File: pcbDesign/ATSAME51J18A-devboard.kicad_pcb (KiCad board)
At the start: 2 copper layers, 82.3 x 28.4 mm, 74 parts, among them J1 Micro_SD_Card, J10 CAN, J11 Conn_01x32_Male, J2 BAT, J3 QWIIC, J7 Conn_01x32_Male, J9 USB4105_REVA, SW1 RST, U1 TCAN1051GVDRQ1, U2 ATSAME51J18A-A, U3 MIC5219-5.0YMM, U4 LM27762, U5 LM2775QDSGTQ1, U6 SC630AULTRT, U7 BQ24074RGT, U8 BQ27441DRZR-G1B, Y1 32.768

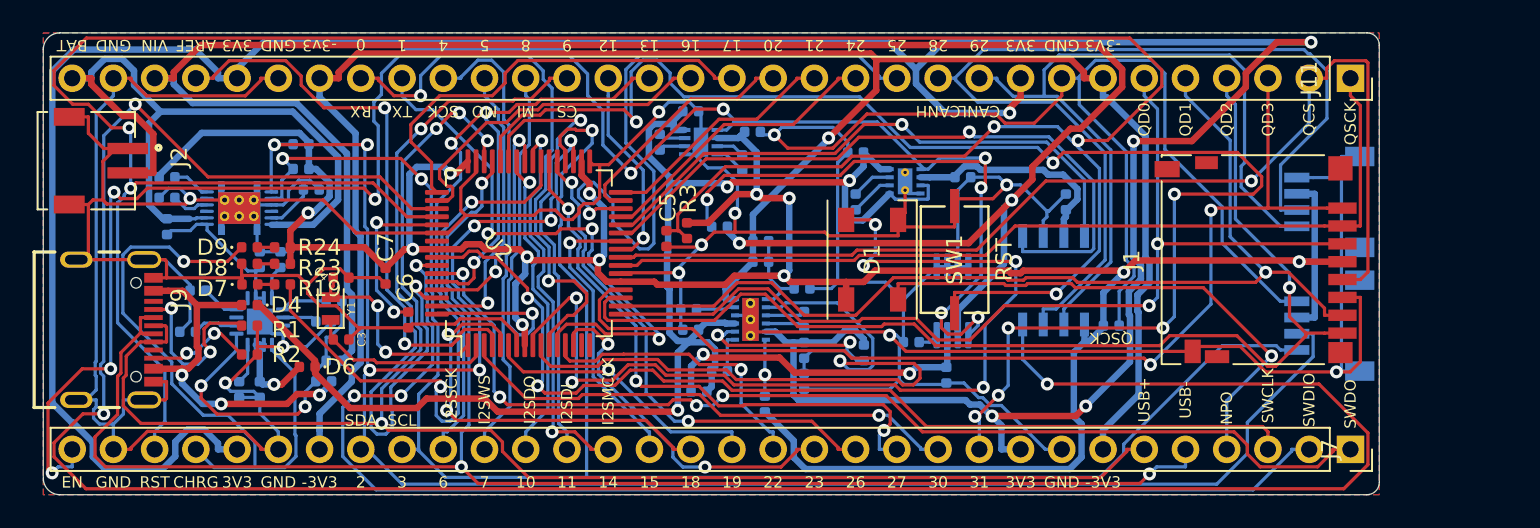
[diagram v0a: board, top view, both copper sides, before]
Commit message: Rewired SD card to SPI for ease of use
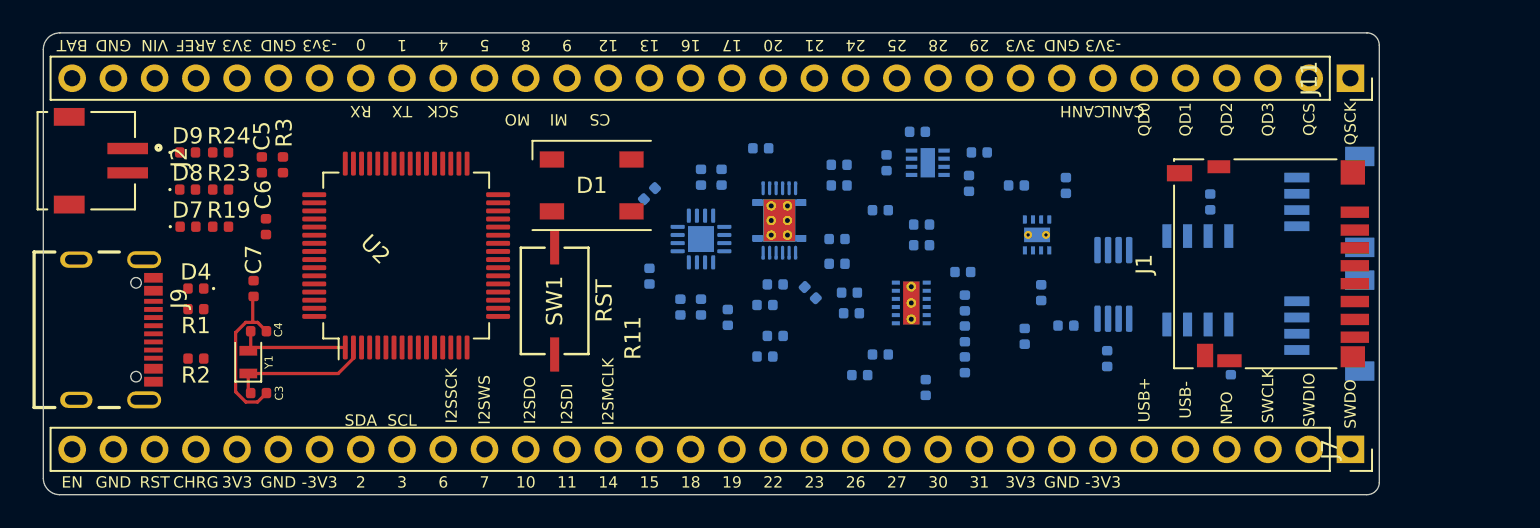
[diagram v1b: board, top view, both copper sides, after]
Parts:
- D6: moved to B.Cu
- moved R17 41.5 mm to (190.0, 119.6), turned to 0 degrees
- moved R18 41.4 mm to (190.0, 120.9), turned to 0 degrees
- moved R16 36.9 mm to (185.2, 118.6), turned to 0 degrees
- moved R14 33.5 mm to (189.9, 124.2)
- moved R15 33.5 mm to (189.9, 125.7)
- moved U8 33.3 mm to (186.3, 123.1), turned to 90 degrees
- moved C24 31.4 mm to (188.2, 127.5), turned to 315 degrees
- moved R11 28.7 mm to (178.3, 126.5), turned to 90 degrees
- moved R13 28.4 mm to (178.3, 121.4), turned to 45 degrees
- moved C22 27.6 mm to (181.5, 128.4)
- moved C23 27.6 mm to (181.5, 120.4)
- moved R22 27.6 mm to (182.8, 120.4)
- moved U7 27.6 mm to (181.5, 124.2)
- moved R12 27.6 mm to (180.2, 128.4)
- moved D2 27.2 mm to (185.4, 131.4)
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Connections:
- J1 pad 1: QDAT3 -> (no net)
- J1 pad 2: QSCK -> SDDAT3
- J1 pad 3: QDAT0 -> 5[MO]
- J1 pad 5: QCS -> 4[SCK]
- J1 pad 7: QDAT1 -> 8[MI]
- J1 pad 8: QDAT2 -> (no net)
- U2 pad 16: (no net) -> SDDAT3
- U5 pad V: GND -> (no net)
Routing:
- net GND: track 446.4 -> 10.0 mm, vias 11 -> 0
- net VBUS_3V3_CH1_REG: track 192.6 -> 0.00 mm, vias 5 -> 0
- net VBUS_3V3_CH0_REG: track 176.2 -> 0.00 mm, vias 12 -> 0
- net RST: track 174.0 -> 0.00 mm, vias 5 -> 0
- net CAN_S: track 155.6 -> 0.00 mm, vias 3 -> 0
- net EN: track 131.6 -> 0.00 mm, vias 11 -> 0
- net VBUS_VIN_NREG: track 128.5 -> 0.00 mm, vias 2 -> 0
- net 2[SDA]: track 124.4 -> 0.00 mm, vias 7 -> 0
- net VBUS_-3V3_CH2_REG: track 119.5 -> 0.00 mm, vias 1 -> 0
- net 3[SCL]: track 116.9 -> 0.00 mm, vias 3 -> 0
- net USB_N: track 101.6 -> 0.00 mm, vias 3 -> 0
- net USB_P: track 99.7 -> 0.00 mm, vias 4 -> 0
- net 31: track 89.8 -> 0.00 mm, vias 7 -> 0
- net VBUS_NREG: track 85.6 -> 0.00 mm, vias 3 -> 0
- net SWDIO: track 78.9 -> 0.00 mm, vias 3 -> 0
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- removed copper zone on B.Cu, net GND
- removed copper zone on F.Cu, net GND

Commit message: Started routing manually
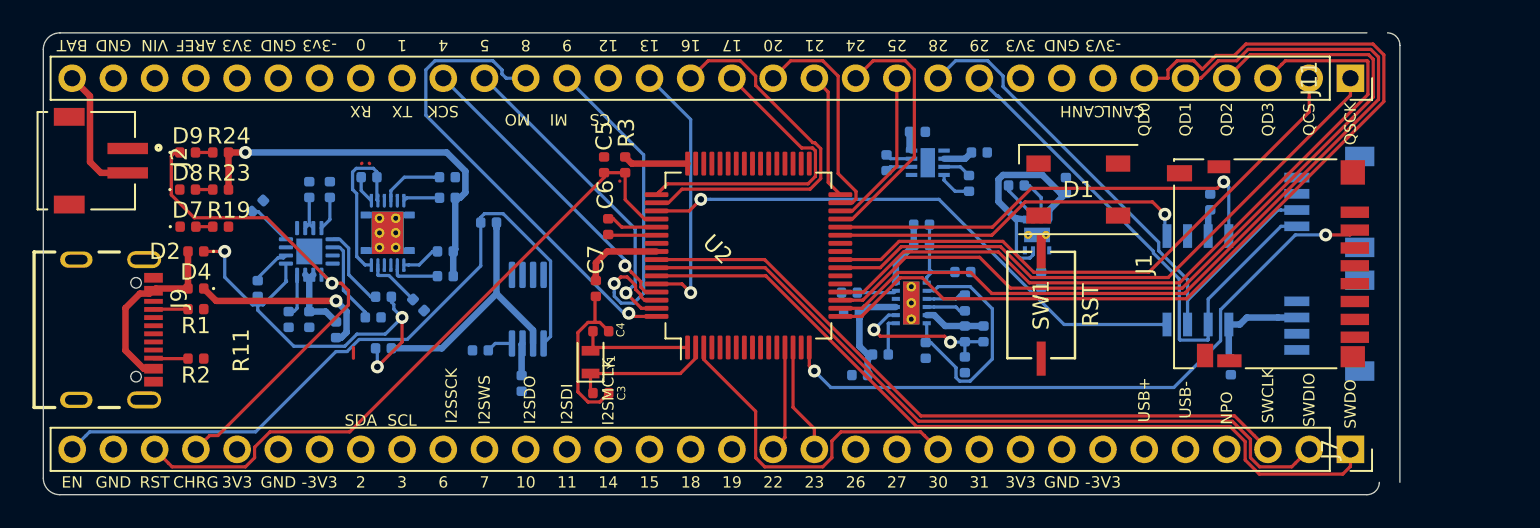
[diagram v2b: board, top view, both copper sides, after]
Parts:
- D2: moved to F.Cu
- moved C12 36.1 mm to (170.4, 133.1)
- moved U3 36.1 mm to (170.8, 128.5)
- moved C8 36.1 mm to (167.9, 131.1)
- moved D2 35.6 mm to (150.4, 125.0), turned to 180 degrees
- moved D1 30.0 mm to (204.7, 121.2)
- moved SW1 30.0 mm to (202.4, 128.3)
- moved R16 24.2 mm to (161.0, 120.4)
- moved R15 24.1 mm to (165.7, 126.5)
- moved R4 24.1 mm to (168.4, 123.2)
- moved C22 24.1 mm to (157.4, 129.2)
- moved C23 24.1 mm to (157.4, 121.2)
- moved C24 24.1 mm to (164.1, 128.3)
- moved D3 24.1 mm to (161.9, 130.9)
- moved D6 24.1 mm to (159.0, 129.8)
- moved R11 24.1 mm to (154.2, 127.3)
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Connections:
- U5 pad V: (no net) -> GND
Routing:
- net QDAT0: track 0.00 -> 59.6 mm
- net QDAT1: track 0.00 -> 55.0 mm
- net QDAT2: track 0.00 -> 51.7 mm
- net SWDO: track 0.00 -> 49.7 mm
- net QDAT3: track 0.00 -> 47.8 mm
- net SWDIO: track 0.00 -> 46.4 mm
- net EN: track 0.00 -> 43.7 mm
- net SWCLK: track 0.00 -> 42.5 mm
- net VBUS_3V3_CH0_REG: track 0.00 -> 41.8 mm, vias 0 -> 1
- net RST: track 0.00 -> 41.6 mm
- net SDDAT3: track 0.00 -> 40.4 mm, vias 0 -> 2
- net QSCK: track 0.00 -> 38.4 mm
- net QCS: track 0.00 -> 36.3 mm
- net CAN_S: track 0.00 -> 34.9 mm, vias 0 -> 1
- net 28[CANH]: track 0.00 -> 33.9 mm
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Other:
- board size 82.3 x 28.4 mm -> 83.6 x 28.4 mm

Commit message: Contnueing routing
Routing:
- net VBUS_-3V3_CH2_REG: track 4.03 -> 108.2 mm, vias 0 -> 6
- net USB_N: track 0.08 -> 86.0 mm
- net USB_P: track 0.04 -> 84.7 mm
- net 4[SCK]: track 19.0 -> 96.2 mm, vias 1 -> 3
- net 8[MI]: track 29.1 -> 100.7 mm, vias 1 -> 2
- net RST: track 41.6 -> 113.2 mm, vias 0 -> 4
- net 5[MO]: track 19.6 -> 89.2 mm, vias 1 -> 2
- net VBUS_3V3_CH1_REG: track 3.77 -> 62.2 mm, vias 0 -> 6
- net 3[SCL]: track 3.12 -> 51.1 mm, vias 0 -> 8
- net 0[Rx0]: track 0.00 -> 44.6 mm, vias 0 -> 4
- net 2[SDA]: track 2.42 -> 46.6 mm, vias 0 -> 6
- net 1[Tx0]: track 0.00 -> 41.8 mm, vias 0 -> 4
- net NEOPIXEL_DOUT: track 0.00 -> 40.2 mm, vias 0 -> 2
- net AREF: track 0.00 -> 39.4 mm, vias 0 -> 1
- net 31: track 0.00 -> 38.3 mm, vias 0 -> 3
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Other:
- outline, holes or cut-outs redrawn

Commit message: Finnished routing for the prototype(v0.1)
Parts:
- moved J2 0.76 mm to (144.0, 120.1)
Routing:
- net VBUS_3V3_CH0_REG: track 77.1 -> 170.1 mm, vias 5 -> 20
- net VBUS_3V3_CH1_REG: track 62.2 -> 139.9 mm, vias 6 -> 8
- net VBUS_NREG: track 33.5 -> 106.1 mm, vias 1 -> 12
- net EN: track 47.0 -> 110.8 mm, vias 0 -> 4
- net 3[SCL]: track 51.1 -> 102.6 mm, vias 8 -> 11
- net 2[SDA]: track 46.6 -> 96.6 mm, vias 6 -> 11
- net 13: track 16.4 -> 55.5 mm, vias 1 -> 6
- net GND: track 13.0 -> 45.5 mm, vias 0 -> 65
- net VBUS_VIN_5V_REG: track 2.00 -> 31.2 mm, vias 0 -> 4
- net VBUS_BAT: track 18.2 -> 43.1 mm, vias 0 -> 1
- net USB_N: track 86.0 -> 109.2 mm, vias 0 -> 4
- net VBUS_-3V3_CH2_REG: track 108.2 -> 130.6 mm, vias 6 -> 11
- net EN_2: track 15.2 -> 36.7 mm, vias 0 -> 5
- net USB_P: track 84.7 -> 102.0 mm, vias 0 -> 6
- net +5V: track 3.01 -> 19.2 mm, vias 0 -> 2
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- added copper zone on B.Cu, net GND
- added copper zone on F.Cu, net GND

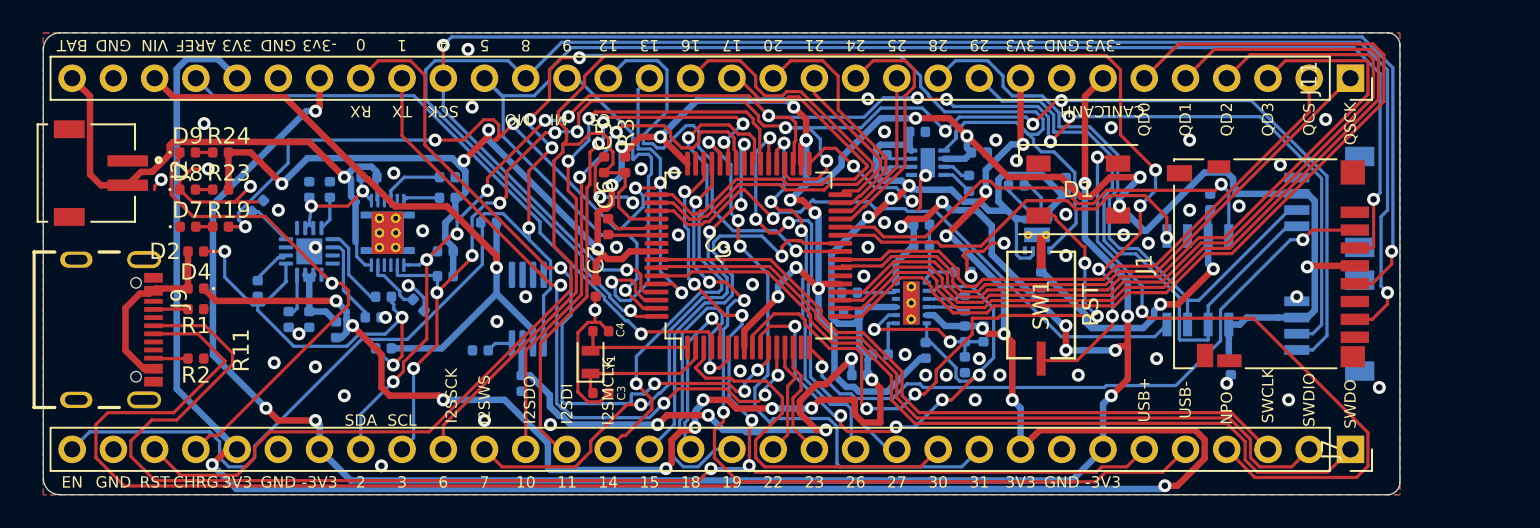
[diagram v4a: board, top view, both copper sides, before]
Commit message: Swapped components for more avaiable ones
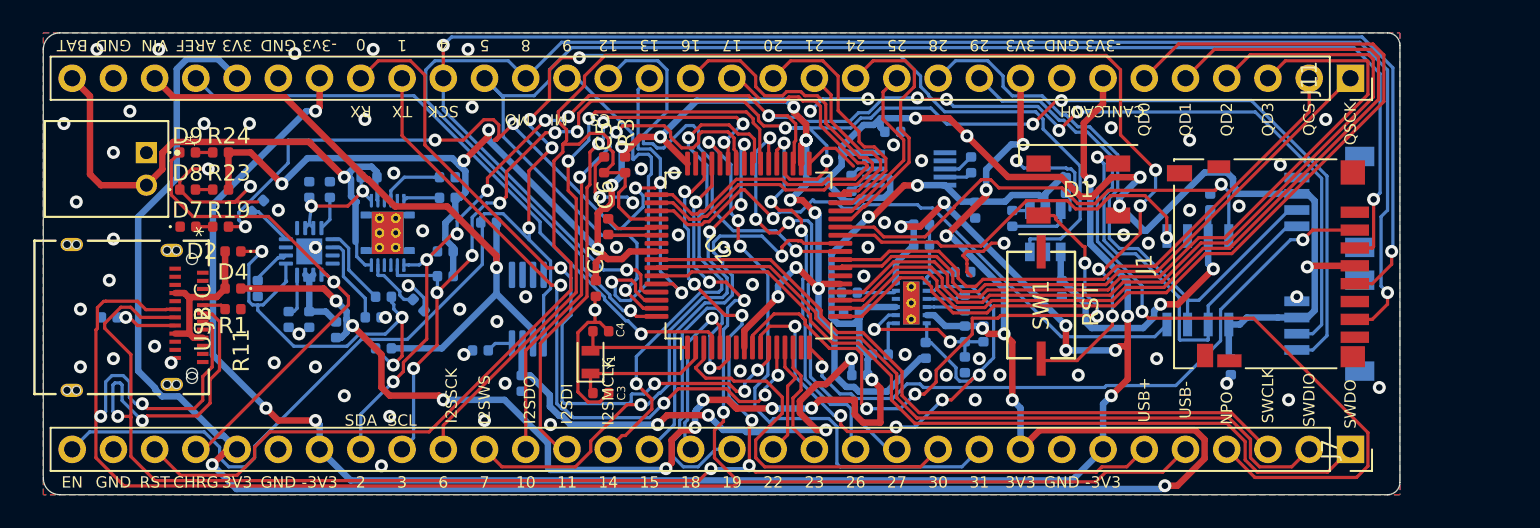
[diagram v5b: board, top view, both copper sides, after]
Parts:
- removed J9: USB4105_REVA, USB4105_REVA:GCT_USB4105_REVA
- removed U6: SC630AULTRT, ul_SC630AULTRT:SC630AULTRT
- added IC1: MP9361DJ-LF-P, SamacSys_Parts:SOT95P280X100-6N, B.Cu at (202.7, 123.7)
- added J4: S2B-PH-K-S(LF)(SN), S2B-PH-K-S_LF__SN_:JST_S2B-PH-K-S(LF)(SN), F.Cu at (147.3, 119.9)
- C10: value 10u -> 2.2u
- C14: value 1u -> 0.47u
- C17, C21: value 2.2u -> 1u
- C20: value 4.7u -> 22u
- J2: value BAT -> USB C; footprint S2B-ZR-SM4A-TF_LF__SN_:JST_S2B-ZR-SM4A-TF(LF)(SN) -> usb_c:12401598E4-2A
- R2: moved to B.Cu
- U5: value LM2775QDSGTQ1 -> TPS60501DGS; footprint ul_LM2775QDSGTQ1:LM2775QDSGTQ1 -> Package_SO:MSOP-10_3x3mm_P0.5mm
- moved J2 9.07 mm to (145.8, 129.0)
- moved U5 8.86 mm to (194.3, 119.9), turned to 180 degrees
- moved C17 7.24 mm to (190.8, 120.8), turned to 90 degrees
- moved R2 5.91 mm to (145.0, 129.0), turned to 180 degrees
- moved C21 5.21 mm to (198.1, 119.6), turned to 90 degrees
- moved C19 3.57 mm to (198.4, 122.4), turned to 270 degrees
- moved D2 2.29 mm to (152.7, 125.0)
- moved D4 2.29 mm to (152.7, 127.3)
- moved R1 2.29 mm to (152.7, 128.5)
- moved C14 2.05 mm to (200.7, 122.9), turned to 270 degrees
- moved C20 1.52 mm to (193.3, 117.6)
- moved C18 1.38 mm to (203.7, 127.3)
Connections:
- C10 pad 1: GND -> VBUS_NREG
- C10 pad 2: VBUS_NREG -> GND
- C19 pad 1: GND -> VBUS_NREG
- C19 pad 2: VBUS_3V3_CH0_REG -> GND
- C20 pad 2: VBUS_NREG -> VBUS_3V3_CH0_REG
- R1 pad 2: Net-(J9-PadA5) -> Net-(J2-PadA5)
- R2 pad 1: Net-(J9-PadB5) -> Net-(J2-PadB5)
- U5 pad 1: VBUS_NREG -> GND
- U5 pad 2: Net-(C14-Pad1) -> (no net)
- U5 pad 3: Net-(C14-Pad2) -> Net-(C21-Pad2)
- U5 pad 4: VBUS_NREG -> Net-(C21-Pad1)
- U5 pad 5: EN -> VBUS_NREG
- U5 pad 6: +5V -> Net-(C17-Pad1)
- U5 pad 7: VBUS_NREG -> VBUS_3V3_CH0_REG
- U5 pad 8: GND -> Net-(C17-Pad2)
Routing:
- net VBUS_NREG: track 106.1 -> 88.2 mm, vias 12 -> 11
- net USB_P: track 102.0 -> 117.9 mm, vias 6 -> 8
- net USB_N: track 109.2 -> 122.9 mm, vias 4 -> 6
- net EN: track 110.8 -> 102.8 mm
- net VBUS_3V3_CH0_REG: track 170.1 -> 177.1 mm
- net Net-(J2-PadB5): track 0.00 -> 3.78 mm, vias 0 -> 1
- net GND: track 45.5 -> 48.5 mm, vias 65 -> 80
- net VBUS_3V3_CH1_REG: track 139.9 -> 142.7 mm
- net Net-(J9-PadB5): track 2.14 -> 0.00 mm
- net Net-(J9-PadA5): track 2.13 -> 0.00 mm
- net VBUS_USB_NREG: track 11.4 -> 9.76 mm
- net Net-(C14-Pad1): track 2.72 -> 1.10 mm
- net Net-(J2-PadA5): track 0.00 -> 1.48 mm
- net Net-(C14-Pad2): track 2.70 -> 3.86 mm
- net 2[SDA]: track 96.6 -> 95.5 mm
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
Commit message: Added logo
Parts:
- added G***: LOGO, Symbol:BatonLogo, F.Cu at (164.1, 126.0)
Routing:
- net GND: vias 80 -> 81
